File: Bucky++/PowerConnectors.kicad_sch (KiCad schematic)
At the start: 15 parts, among them J1 XT60PW-M, J11 XT30AW-M, J12 XT30AW-M, J13 XT30AW-M, J14 XT30AW-M, J17 XT30UPB-F, J18 XT30UPB-F, J2 XT60PW-F, J3 XT30PW-F, J4 XT30PW-F, J5 XT30PW-F, J6 XT30PW-F, J7 XT30UPB-F, J8 XT30UPB-F

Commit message: final version before review
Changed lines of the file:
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@@
+	)
+	(junction
+		(at 57.15 90.17)
+		(diameter 0)
+		(color 0 0 0 0)
 	)
 	(junction
@@
 	(wire
 		(pts
+			(xy 58.42 83.82) (xy 63.5 83.82)
+		)
+		(stroke
+			(width 0)
+			(type default)
+		)
+	)
+	(wire
+		(pts
 			(xy 165.1 46.99) (xy 173.99 46.99)
 		)
@@
 	(wire
 		(pts
+			(xy 58.42 90.17) (xy 58.42 83.82)
+		)
+		(stroke
+			(width 0)
+			(type default)
+		)
+	)
+	(wire
+		(pts
 			(xy 110.49 46.99) (xy 118.11 46.99)
 		)
@@
 	(wire
 		(pts
-			(xy 57.15 83.82) (xy 63.5 83.82)
+			(xy 57.15 90.17) (xy 58.42 90.17)
 		)
 		(stroke
@@
 	(symbol
 		(lib_id "power:GND")
-		(at 57.15 83.82 0)
+		(at 57.15 90.17 0)
 		(unit 1)
 		(exclude_from_sim no)
@@
 		(fields_autoplaced yes)
 		(property "Reference" "#PWR025"
+			(at 57.15 96.52 0)
+			(effects
+				(font
+					(size 1.27 1.27)
+				)
+				(hide yes)
+			)
+		)
+		(property "Value" "GND"
+			(at 57.15 95.25 0)
+			(effects
+				(font
+					(size 1.27 1.27)
+				)
+			)
+		)
+		(property "Footprint" ""
 			(at 57.15 90.17 0)
 			(effects
@@
 			)
 		)
-		(property "Value" "GND"
-			(at 57.15 88.9 0)
-			(effects
-				(font
-					(size 1.27 1.27)
-				)
-			)
-		)
-		(property "Footprint" ""
-			(at 57.15 83.82 0)
-			(effects
-				(font
-					(size 1.27 1.27)
-				)
-				(hide yes)
-			)
-		)
 		(property "Datasheet" ""
-			(at 57.15 83.82 0)
+			(at 57.15 90.17 0)
 			(effects
 				(font
@@
 		)
 		(property "Description" "Power symbol creates a global label with name \"GND\" , ground"
-			(at 57.15 83.82 0)
+			(at 57.15 90.17 0)
 			(effects
 				(font
@@
 					(unit 1)
 				)
+			)
+		)
+	)
+	(symbol
+		(lib_id "power:PWR_FLAG")
+		(at 57.15 90.17 0)
+		(unit 1)
+		(exclude_from_sim no)
+		(in_bom yes)
+		(on_board yes)
+		(dnp no)
+		(fields_autoplaced yes)
+		(property "Reference" "#FLG08"
+			(at 57.15 88.265 0)
+			(effects
+				(font
+					(size 1.27 1.27)
+				)
+				(hide yes)
+			)
+		)
+		(property "Value" "PWR_FLAG"
+			(at 57.15 85.09 0)
+			(effects
+				(font
+					(size 1.27 1.27)
+				)
+			)
+		)
+		(property "Footprint" ""
+			(at 57.15 90.17 0)
+			(effects
+				(font
+					(size 1.27 1.27)
+				)
+				(hide yes)
+			)
+		)
+		(property "Datasheet" "~"
+			(at 57.15 90.17 0)
+			(effects
+				(font
+					(size 1.27 1.27)
+				)
+				(hide yes)
+			)
+		)
+		(property "Description" "Special symbol for telling ERC where power comes from"
+			(at 57.15 90.17 0)
+			(effects
+				(font
+					(size 1.27 1.27)
+				)
+				(hide yes)
+			)
+		)
+		(pin "1"
+		)
+		(instances
+			(project "Bucky++"
+				(path "/0650c7a8-acba-429c-9f8e-eec0baf0bc1c/fede4c36-00cc-4d3d-b71c-5243ba232202/0b884d20-85c8-4e14-bcd5-df65213f1de9"
+					(reference "#FLG08")
+					(unit 1)
+				)

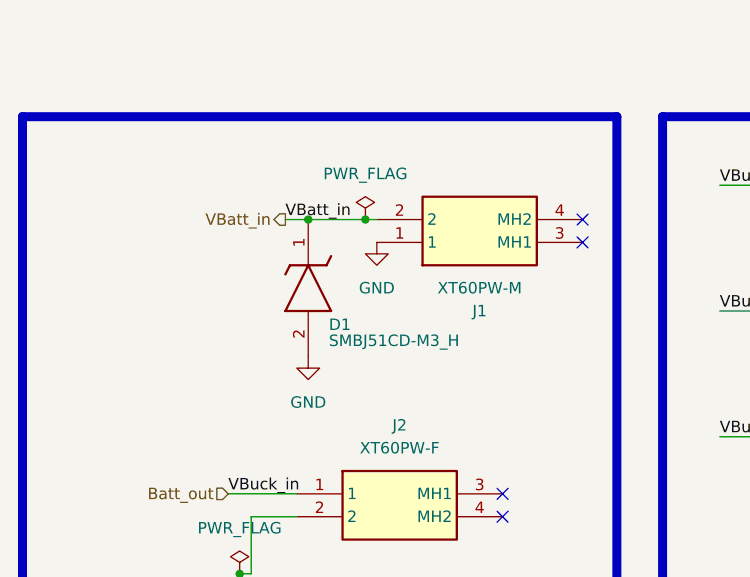
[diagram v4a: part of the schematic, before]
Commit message: initial component placement
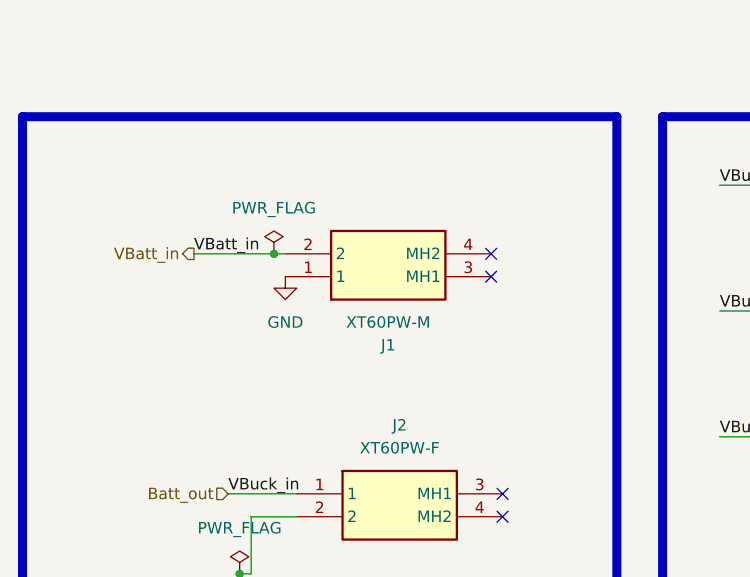
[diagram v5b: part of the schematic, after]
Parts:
- removed D1: SMBJ51CD-M3_H, SamacSys_Parts:DIOM5436X244N, symbol SamacSys_Parts:SMBJ51CD-M3_H
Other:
- moved on the sheet: J1

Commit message: worked on layout, added adm1270
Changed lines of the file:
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@@
+	)
+	(bus_entry
+		(at 231.14 134.62)
+		(size 2.54 -2.54)
+		(stroke
+			(width 0)
+			(type default)
+		)
+	)
+	(bus_entry
+		(at 231.14 142.24)
+		(size 2.54 -2.54)
+		(stroke
+			(width 0)
+			(type default)
+		)
+	)
+	(bus_entry
+		(at 231.14 139.7)
+		(size 2.54 -2.54)
+		(stroke
+			(width 0)
+			(type default)
+		)
 	)
 	(bus_entry
 		(at 231.14 137.16)
-		(size -2.54 2.54)
-		(stroke
-			(width 0)
-			(type default)
-		)
-	)
-	(bus_entry
-		(at 231.14 142.24)
-		(size -2.54 2.54)
+		(size 2.54 -2.54)
 		(stroke
 			(width 0)
@@
 	)
 	(bus_entry
-		(at 231.14 127)
-		(size -2.54 2.54)
-		(stroke
-			(width 0)
-			(type default)
-		)
-	)
-	(bus_entry
 		(at 179.07 132.08)
 		(size -2.54 2.54)
@@
 	)
 	(bus_entry
-		(at 231.14 132.08)
-		(size -2.54 2.54)
-		(stroke
-			(width 0)
-			(type default)
-		)
-	)
-	(bus_entry
 		(at 179.07 137.16)
 		(size -2.54 2.54)
@@
 		)
 	)
-	(bus
-		(pts
-			(xy 231.14 127) (xy 231.14 123.19)
-		)
-		(stroke
-			(width 0)
-			(type default)
-		)
-	)
 	(wire
 		(pts
@@
 		)
 	)
-	(bus
-		(pts
-			(xy 231.14 142.24) (xy 231.14 137.16)
-		)
-		(stroke
-			(width 0)
-			(type default)
-		)
-	)
-	(wire
-		(pts
-			(xy 220.98 134.62) (xy 228.6 134.62)
-		)
-		(stroke
-			(width 0)
-			(type default)
-		)
-	)
 	(wire
 		(pts
@@
 		)
 	)
+	(wire
+		(pts
+			(xy 228.6 139.7) (xy 231.14 139.7)
+		)
+		(stroke
+			(width 0)
+			(type default)
+		)
+	)
+	(wire
+		(pts
+			(xy 228.6 134.62) (xy 231.14 134.62)
+		)
+		(stroke
+			(width 0)
+			(type default)
+		)
+	)
 	(bus
 		(pts
@@
 	(wire
 		(pts
-			(xy 220.98 129.54) (xy 228.6 129.54)
-		)
-		(stroke
-			(width 0)
-			(type default)
-		)
-	)
-	(wire
-		(pts
 			(xy 55.88 81.28) (xy 63.5 81.28)
 		)
@@
 	(bus
 		(pts
-			(xy 231.14 123.19) (xy 238.76 123.19)
+			(xy 233.68 130.81) (xy 237.49 130.81)
 		)
 		(stroke
@@
 		)
 	)
+	(bus
+		(pts
+			(xy 233.68 139.7) (xy 233.68 137.16)
+		)
+		(stroke
+			(width 0)
+			(type default)
+		)
+	)
 	(wire
 		(pts
@@
 		)
 	)
-	(bus
-		(pts
-			(xy 231.14 137.16) (xy 231.14 132.08)
+	(wire
+		(pts
+			(xy 228.6 137.16) (xy 231.14 137.16)
 		)
 		(stroke
@@
 		)
 	)
-	(bus
-		(pts
-			(xy 231.14 132.08) (xy 231.14 127)
-		)
-		(stroke
-			(width 0)
-			(type default)
-		)
-	)
 	(wire
 		(pts
@@
 		)
 	)
+	(bus
+		(pts
+			(xy 233.68 137.16) (xy 233.68 134.62)
+		)
+		(stroke
+			(width 0)
+			(type default)
+		)
+	)
+	(bus
+		(pts
+			(xy 233.68 132.08) (xy 233.68 130.81)
+		)
+		(stroke
+			(width 0)
+			(type default)
+		)
+	)
 	(wire
 		(pts
@@
 	(wire
 		(pts
-			(xy 220.98 144.78) (xy 228.6 144.78)
-		)
-		(stroke
-			(width 0)
-			(type default)
-		)
-	)
-	(wire
-		(pts
 			(xy 224.79 49.53) (xy 231.14 49.53)
 		)
@@
 	(wire
 		(pts
-			(xy 220.98 139.7) (xy 228.6 139.7)
-		)
-		(stroke
-			(width 0)
-			(type default)
-		)
-	)
-	(wire
-		(pts
 			(xy 168.91 139.7) (xy 176.53 139.7)
 		)
@@
 		(pts
 			(xy 179.07 127) (xy 179.07 123.19)
+		)
+		(stroke
+			(width 0)
+			(type default)
+		)
+	)
+	(bus
+		(pts
+			(xy 233.68 134.62) (xy 233.68 132.08)
+		)
+		(stroke
+			(width 0)
+			(type default)
+		)
+	)
+	(wire
+		(pts
+			(xy 228.6 142.24) (xy 231.14 142.24)
 		)
 		(stroke
@@
 		)
 	)
+	(label "12V_safe"
+		(at 228.6 137.16 180)
+		(effects
+			(font
+				(size 1.27 1.27)
+			)
+			(justify right bottom)
+		)
+	)
+	(label "15V_safe"
+		(at 228.6 139.7 180)
+		(effects
+			(font
+				(size 1.27 1.27)
+			)
+			(justify right bottom)
+		)
+	)
 	(label "Vin_5V"
 		(at 168.91 129.54 0)
@@
 	)
 	(label "out24V"
-		(at 220.98 144.78 0)
-		(effects
-			(font
-				(size 1.27 1.27)
-			)
-			(justify left bottom)
-		)
-	)
-	(label "out24V"
 		(at 222.25 92.71 0)
 		(effects
@@
 		)
 	)
+	(label "5V_safe"
+		(at 228.6 134.62 180)
+		(effects
+			(font
+				(size 1.27 1.27)
+			)
+			(justify right bottom)
+		)
+	)
 	(label "VBuck_in"
 		(at 110.49 46.99 0)
@@
 		)
 	)
-	(label "out5V"
-		(at 220.98 129.54 0)
-		(effects
-			(font
-				(size 1.27 1.27)
-			)
-			(justify left bottom)
-		)
-	)
 	(label "VBuck_in"
 		(at 110.49 74.93 0)
@@
 		)
 	)
-	(label "out12V"
-		(at 220.98 134.62 0)
-		(effects
-			(font
-				(size 1.27 1.27)
-			)
-			(justify left bottom)
-		)
-	)
 	(label "VBuck_in"
 		(at 110.49 92.71 0)
@@
 		)
 	)
-	(label "out15V"
-		(at 220.98 139.7 0)
-		(effects
-			(font
-				(size 1.27 1.27)
-			)
-			(justify left bottom)
+	(label "24V_safe"
+		(at 228.6 142.24 180)
+		(effects
+			(font
+				(size 1.27 1.27)
+			)
+			(justify right bottom)
 		)
 	)
@@
 			)
 			(justify left bottom)
-		)
-	)
-	(hierarchical_label "{Shunt_Outputs}"
-		(shape tri_state)
-		(at 238.76 123.19 0)
-		(effects
-			(font
-				(size 1.27 1.27)
-			)
-			(justify left)
 		)
 	)
@@
 		(effects
 			(font
+				(size 1.27 1.27)
+			)
+			(justify left)
+		)
+	)
+	(hierarchical_label "{Safe_Outputs}"
+		(shape tri_state)
+		(at 237.49 130.81 0)
+		(effects
+			(font

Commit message: more routing
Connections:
- net out12V is gone; now on net 12V_safe: J4.2
- net out15V is gone; now on net 15V_safe: J5.2
- net out24V is gone; now on net 24V_safe: J6.2
- net out5V is gone; now on net 5V_safe: J3.2
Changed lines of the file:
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@@
-		)
-	)
-	(label "out5V"
-		(at 220.98 46.99 0)
-		(effects
-			(font
-				(size 1.27 1.27)
-			)
-			(justify left bottom)
 		)
 	)
@@
 		)
 	)
-	(label "out24V"
-		(at 222.25 92.71 0)
-		(effects
-			(font
-				(size 1.27 1.27)
-			)
-			(justify left bottom)
+	(label "5V_safe"
+		(at 220.98 46.99 180)
+		(effects
+			(font
+				(size 1.27 1.27)
+			)
+			(justify right bottom)
 		)
 	)
@@
 		)
 	)
-	(label "out15V"
-		(at 222.25 77.47 0)
-		(effects
-			(font
-				(size 1.27 1.27)
-			)
-			(justify left bottom)
-		)
-	)
 	(label "5V_safe"
 		(at 228.6 134.62 180)
@@
 		)
 	)
-	(label "out12V"
-		(at 220.98 62.23 0)
-		(effects
-			(font
-				(size 1.27 1.27)
-			)
-			(justify left bottom)
-		)
-	)
 	(label "Vin_12V"
 		(at 168.91 134.62 0)
@@
 		)
 	)
+	(label "24V_safe"
+		(at 222.25 92.71 180)
+		(effects
+			(font
+				(size 1.27 1.27)
+			)
+			(justify right bottom)
+		)
+	)
 	(label "VBuck_in"
 		(at 110.49 92.71 0)
@@
 		)
 	)
+	(label "12V_safe"
+		(at 220.98 62.23 180)
+		(effects
+			(font
+				(size 1.27 1.27)
+			)
+			(justify right bottom)
+		)
+	)
+	(label "15V_safe"
+		(at 222.25 77.47 180)
+		(effects
+			(font
+				(size 1.27 1.27)
+			)
+			(justify right bottom)
+		)
+	)

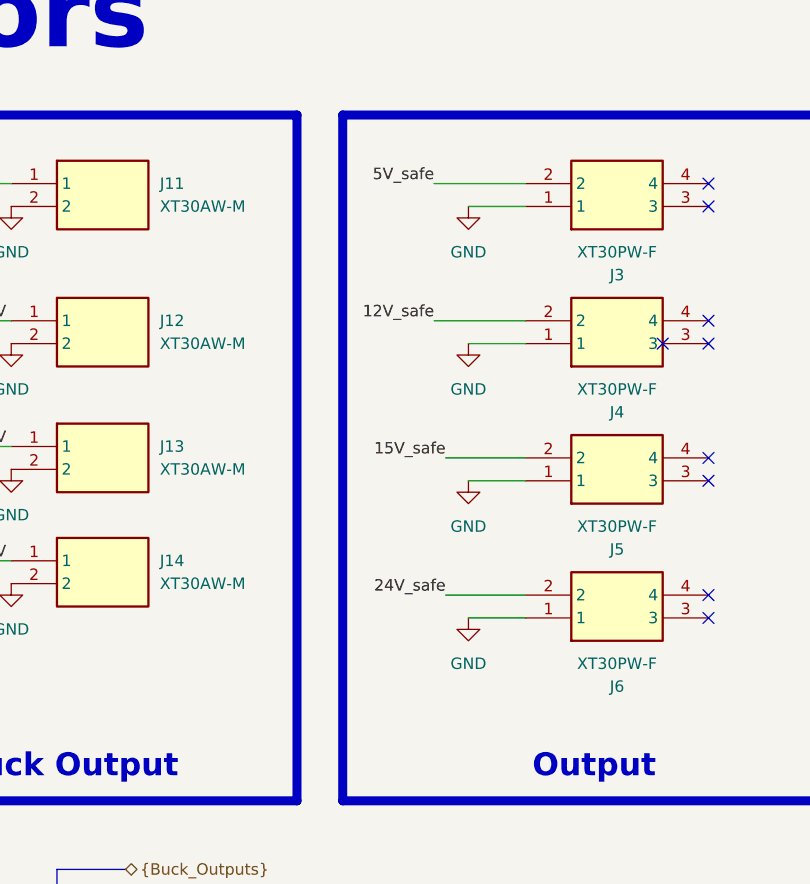
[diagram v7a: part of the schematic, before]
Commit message: updated circuit after review. updated silkscreen
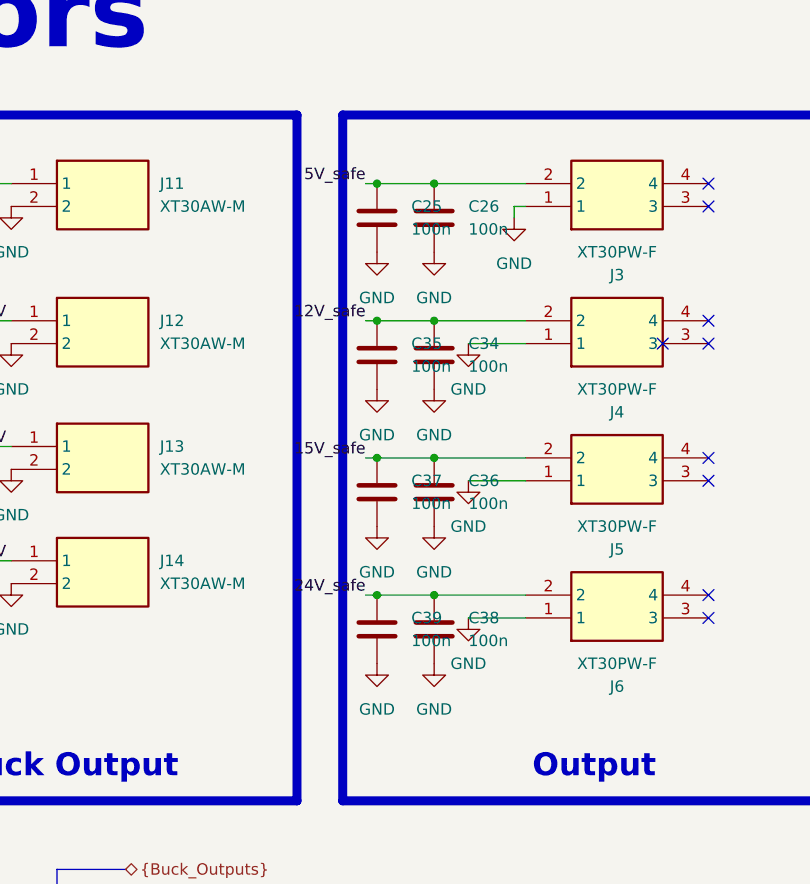
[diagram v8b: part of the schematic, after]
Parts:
- added C25, C26, C34, C35, C36, C37, C38, C39: 100n, Capacitor_SMD:C_1812_4532Metric_Pad1.57x3.40mm_HandSolder, symbol Device:C
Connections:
- net 12V_safe: now also C34.1, C35.1
- net 15V_safe: now also C36.1, C37.1
- net 24V_safe: now also C38.1, C39.1
- net 5V_safe: now also C25.1, C26.1
- net GND: now also C25.2, C26.2, C34.2, C35.2, C36.2, C37.2, C38.2, C39.2
